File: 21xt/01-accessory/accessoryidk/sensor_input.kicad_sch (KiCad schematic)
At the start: 29 parts, among them IC4 AD7175-8BCPZ-RL7, IC5 INA821IDGKT, IC6 TXB0108PWR, IC8 INA821IDGKT, IC9 INA821IDGKT, J2 Conn_01x25

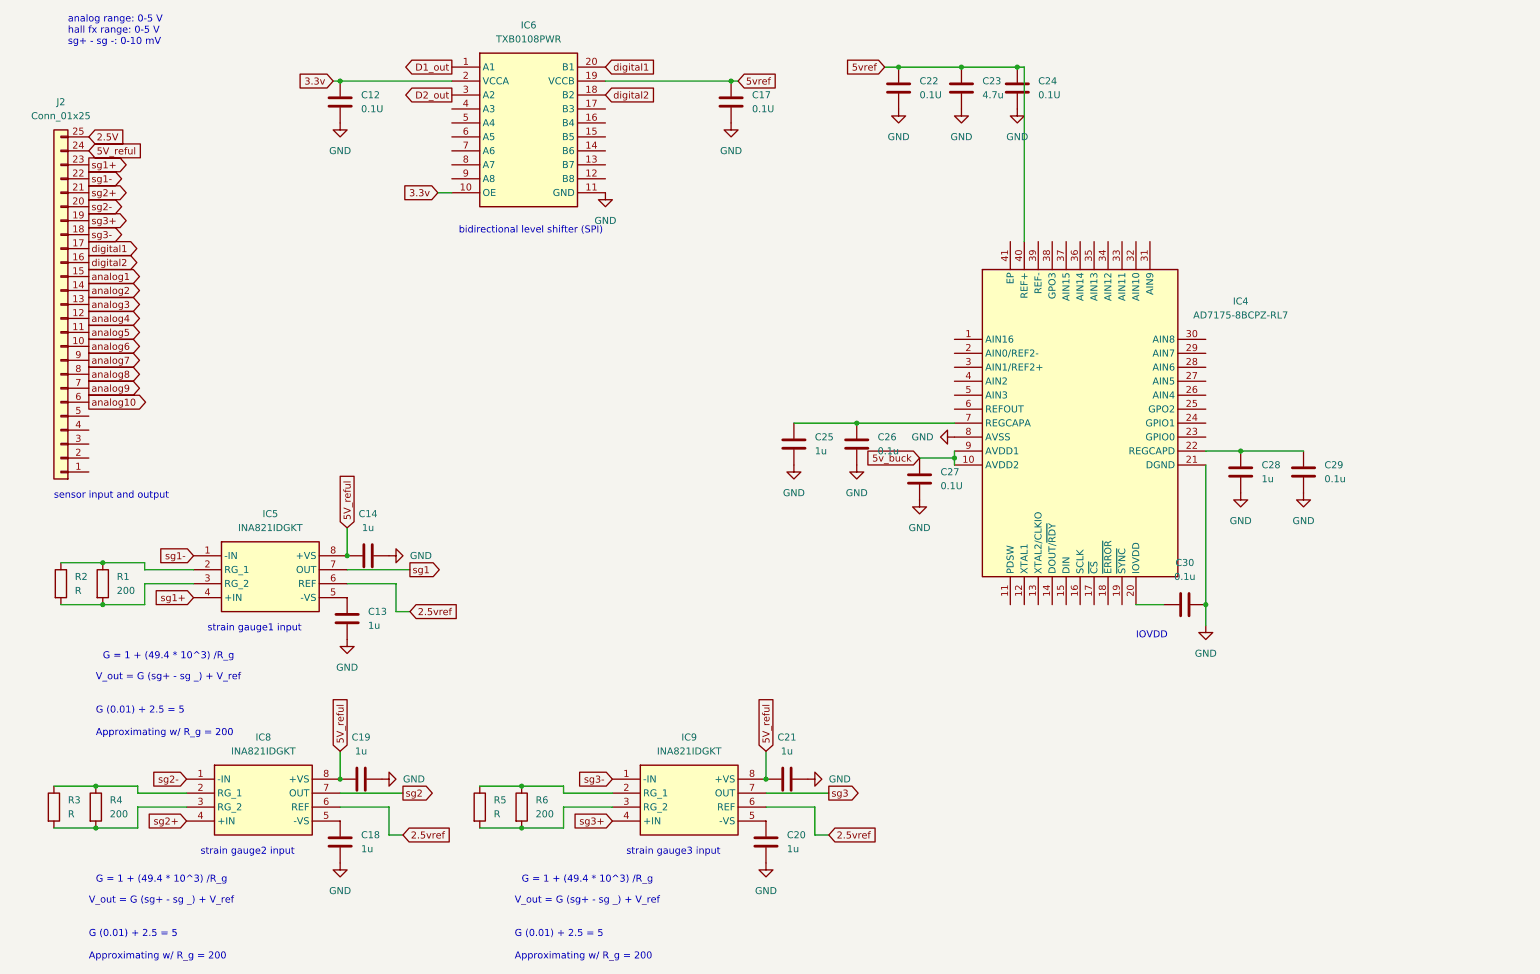
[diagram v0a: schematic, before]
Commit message: Unfinished V1 accessory schematic, remaining teensy connections
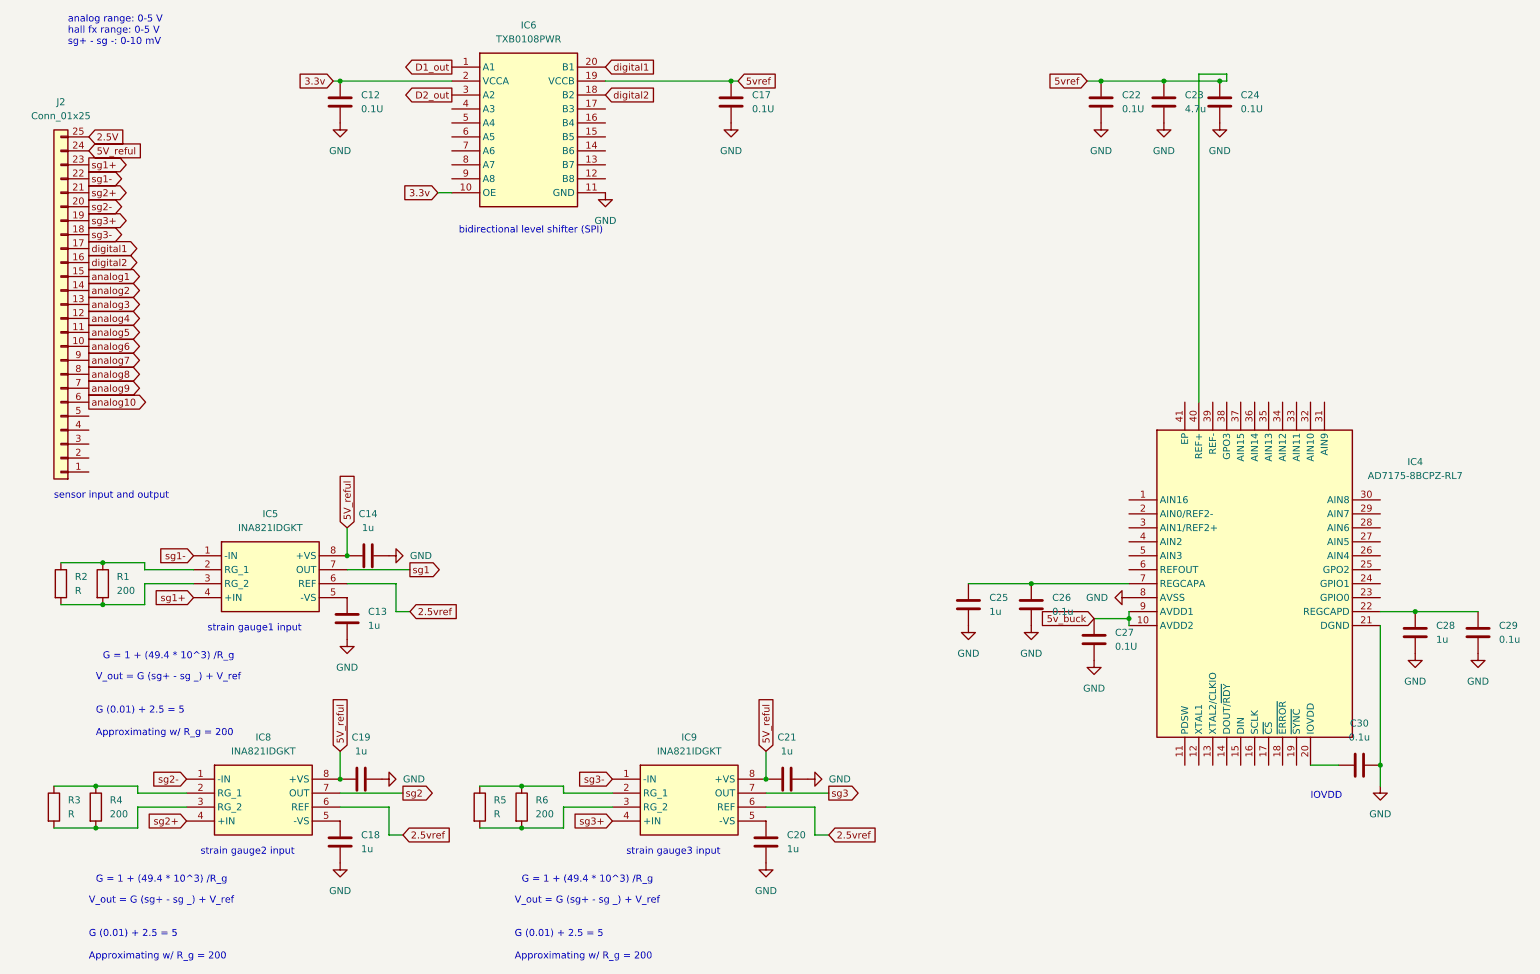
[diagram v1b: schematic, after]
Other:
- moved on the sheet: C22, C23, C24, C25, C26, C27, C28, C29, C30, IC4

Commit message: Unfinished V1 accessory schematic, adding teensy ADC connections part 1
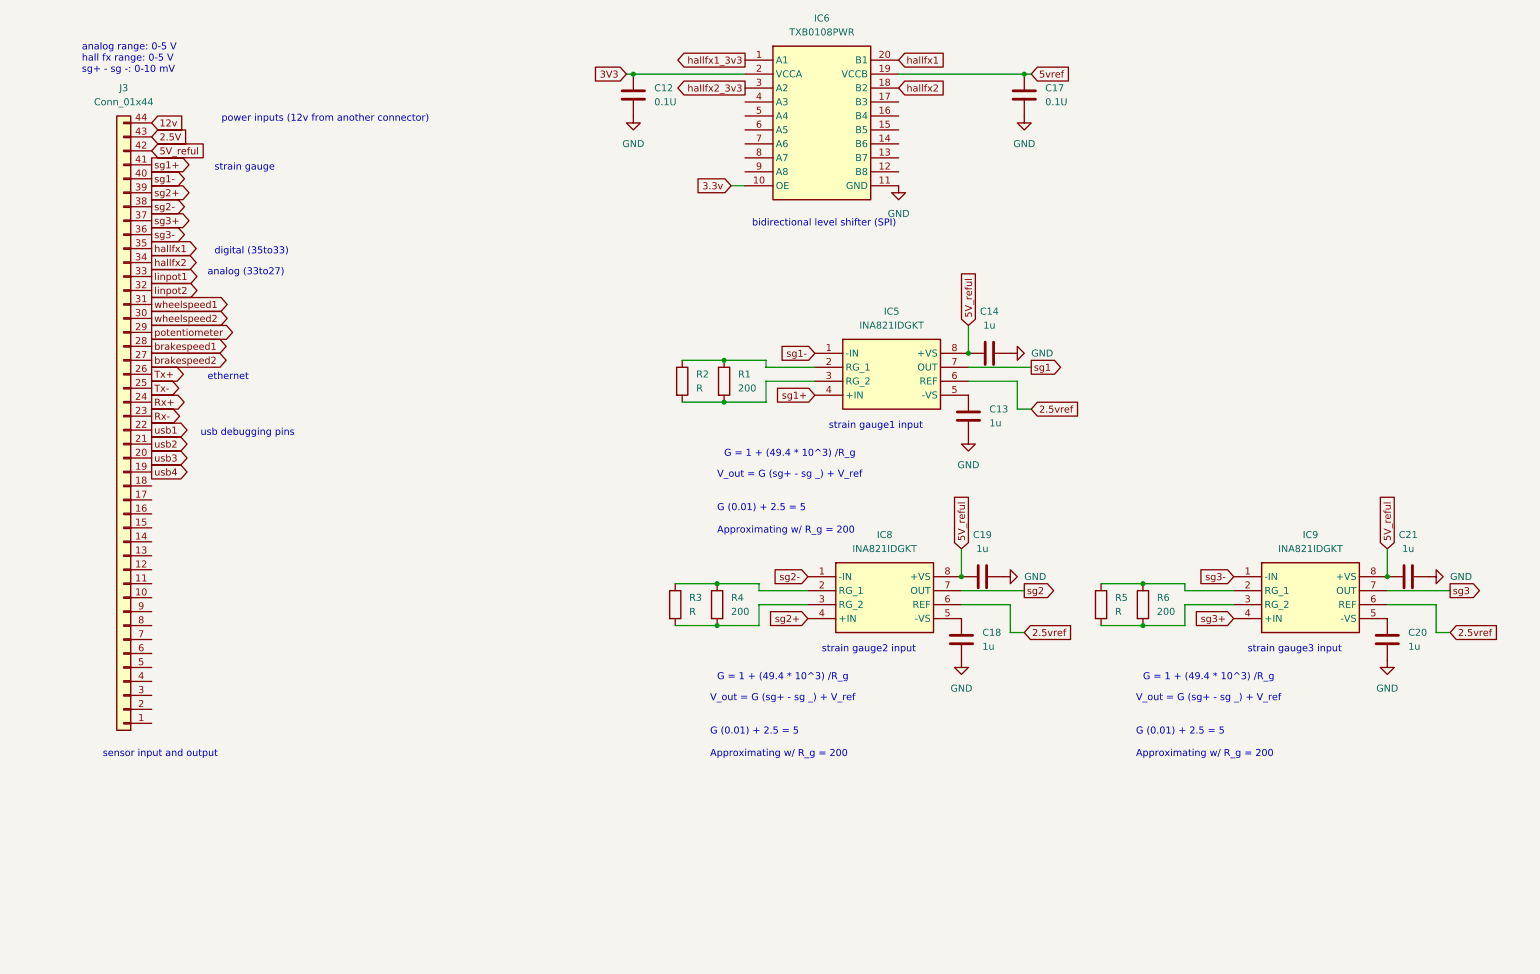
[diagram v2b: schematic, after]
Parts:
- removed C22, C24, C27: 0.1U, symbol Device:C
- removed C23: 4.7u, symbol Device:C
- removed C25, C28: 1u, symbol Device:C
- removed C26, C29, C30: 0.1u, symbol Device:C
- removed IC4: AD7175-8BCPZ-RL7, QFN50P600X600X80-41N-D, symbol 21xt_symbols:AD7175-8BCPZ-RL7
- removed J2: Conn_01x25, symbol Connector_Generic:Conn_01x25
- added J3: Conn_01x44, symbol Connector_Generic:Conn_01x44
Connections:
- net 2.5V: now also J3.43 (Pin_43)
- net 3.3v: no longer C12.1, IC6.2 (VCCA)
- net 5V_reful: now also J3.42 (Pin_42)
- net sg1+: now also J3.41 (Pin_41)
- net sg1-: now also J3.40 (Pin_40)
- net sg2+: now also J3.39 (Pin_39)
- net sg2-: now also J3.38 (Pin_38)
- net sg3+: now also J3.37 (Pin_37)
- net sg3-: now also J3.36 (Pin_36)
- net D1_out renamed hallfx1_3v3
- net D2_out renamed hallfx2_3v3
- net digital1 renamed hallfx1
- net hallfx1: now also J3.35 (Pin_35)
- net digital2 renamed hallfx2
- net hallfx2: now also J3.34 (Pin_34)
- new net 12v: J3.44 (Pin_44)
- new net 3V3: C12.1, IC6.2 (VCCA)
- new net Rx+: J3.24 (Pin_24)
- new net Rx-: J3.23 (Pin_23)
- new net Tx+: J3.26 (Pin_26)
- new net Tx-: J3.25 (Pin_25)
- new net brakespeed1: J3.28 (Pin_28)
- new net brakespeed2: J3.27 (Pin_27)
- new net linpot1: J3.33 (Pin_33)
- new net linpot2: J3.32 (Pin_32)
- new net potentiometer: J3.29 (Pin_29)
- new net usb1: J3.22 (Pin_22)
- new net usb2: J3.21 (Pin_21)
- new net usb3: J3.20 (Pin_20)
- new net usb4: J3.19 (Pin_19)
- new net wheelspeed1: J3.31 (Pin_31)
- new net wheelspeed2: J3.30 (Pin_30)
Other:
- note added: "analog (33to27)"
- note added: "digital (35to33)"
- note added: "ethernet"
- note added: "power inputs (12v from another connector)"
- note added: "strain gauge"
- note added: "usb debugging pins"
- note removed: "IOVDD"
- moved on the sheet: C12, C13, C14, C17, C18, C19, C20, C21, IC5, IC6, IC8, IC9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

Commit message: Finished V1 schematic, adding footprints
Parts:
- added J2: Conn_01x44, symbol Connector_Generic:Conn_01x44
- C12, C17: value 0.1U -> 0.1u; footprint (none) -> Capacitor_SMD:C_0603_1608Metric
- C13, C14, C18, C19, C20, C21: footprint (none) -> Capacitor_SMD:C_0603_1608Metric
- IC5, IC8, IC9: footprint SOP65P490X110-8N -> (none)
- IC6: footprint SOP65P640X120-20N -> (none)
- R1, R2, R3, R4, R5, R6: footprint (none) -> Resistor_SMD:R_0603_1608Metric
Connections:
- net usb1 is gone; now on net sg1-: J3.22 (Pin_22)
- net usb2 is gone; now on net sg2+: J3.21 (Pin_21)
- net usb3 is gone; now on net sg2-: J3.20 (Pin_20)
- net usb4 is gone; now on net sg3+: J3.19 (Pin_19)
- net 12v: now also J2.44 (Pin_44)
- net 2.5V: now also J2.43 (Pin_43)
- net 5V_reful: now also J2.42 (Pin_42)
- net GND: no longer C13.2, C14.2, C18.2, C19.2, C20.2, C21.2
- net Rx+: now also J3.6 (Pin_6), J2.6 (Pin_6); no longer J3.24 (Pin_24)
- net Rx-: now also J3.5 (Pin_5), J2.5 (Pin_5); no longer J3.23 (Pin_23)
- net Tx+: now also J3.8 (Pin_8), J2.8 (Pin_8); no longer J3.26 (Pin_26)
- net Tx-: now also J3.7 (Pin_7), J2.7 (Pin_7); no longer J3.25 (Pin_25)
- net brakespeed1: now also J3.10 (Pin_10), J2.10 (Pin_10); no longer J3.28 (Pin_28)
- net brakespeed2: now also J3.9 (Pin_9), J2.9 (Pin_9); no longer J3.27 (Pin_27)
- net hallfx1: now also J3.17 (Pin_17), J2.17 (Pin_17); no longer J3.35 (Pin_35)
- net hallfx2: now also J3.16 (Pin_16), J2.16 (Pin_16); no longer J3.34 (Pin_34)
- net linpot1: now also J3.15 (Pin_15), J2.15 (Pin_15); no longer J3.33 (Pin_33)
- net linpot2: now also J3.14 (Pin_14), J2.14 (Pin_14); no longer J3.32 (Pin_32)
- net potentiometer: now also J3.11 (Pin_11), J2.11 (Pin_11); no longer J3.29 (Pin_29)
- net sg1+: now also J3.23 (Pin_23), J2.23 (Pin_23); no longer J3.41 (Pin_41)
- net sg1-: now also J2.22 (Pin_22); no longer J3.40 (Pin_40)
- net sg2+: now also J2.21 (Pin_21); no longer J3.39 (Pin_39)
- net sg2-: now also J2.20 (Pin_20); no longer J3.38 (Pin_38)
- net sg3+: now also J2.19 (Pin_19); no longer J3.37 (Pin_37)
- net sg3-: now also J3.18 (Pin_18), J2.18 (Pin_18); no longer J3.36 (Pin_36)
- net wheelspeed1: now also J3.13 (Pin_13), J2.13 (Pin_13); no longer J3.31 (Pin_31)
- net wheelspeed2: now also J3.12 (Pin_12), J2.12 (Pin_12); no longer J3.30 (Pin_30)
- net GNDA: now reaches J3.1 (Pin_1)
- net GNDA: now also C13.2, C14.2, C18.2, C19.2, C20.2, C21.2, J2.1 (Pin_1)
- net usb_d+: now reaches J3.2 (Pin_2)
- net usb_d+: now also J2.2 (Pin_2)
- net usb_d-: now reaches J3.3 (Pin_3)
- net usb_d-: now also J2.3 (Pin_3)
- net 5v_buck: now reaches J3.4 (Pin_4)
- net 5v_buck: now also J2.4 (Pin_4)
- new net GNDD: J2.24 (Pin_24), J2.25 (Pin_25), J2.26 (Pin_26), J2.27 (Pin_27), J2.28 (Pin_28), J2.29 (Pin_29), J2.30 (Pin_30), J2.31 (Pin_31), J2.32 (Pin_32), J2.33 (Pin_33), J2.34 (Pin_34), J2.35 (Pin_35), J2.36 (Pin_36), J2.37 (Pin_37), J2.38 (Pin_38), J2.39 (Pin_39), J2.40 (Pin_40), J2.41 (Pin_41), J3.24 (Pin_24), J3.25 (Pin_25), J3.26 (Pin_26), J3.27 (Pin_27), J3.28 (Pin_28), J3.29 (Pin_29), J3.30 (Pin_30), J3.31 (Pin_31), J3.32 (Pin_32), J3.33 (Pin_33), J3.34 (Pin_34), J3.35 (Pin_35), J3.36 (Pin_36), J3.37 (Pin_37), J3.38 (Pin_38), J3.39 (Pin_39), J3.40 (Pin_40), J3.41 (Pin_41)
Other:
- note added: "sensor input and output (db44)"
- note added: "sensor input and output (dupont testing)"
- note removed: "sensor input and output"
- moved on the sheet: J3

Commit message: Accessory V1 unfinished layout
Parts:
- removed J2, J3: Conn_01x44, symbol Connector_Generic:Conn_01x44
- added J2: DB-44 Connector, 21xt_footprints:23117702, symbol 21xt_symbols:2311770-2
- added J3, J4, J5, J6: Conn_01x11, Connector_JST:JST_EH_B11B-EH-A_1x11_P2.50mm_Vertical, symbol Connector_Generic:Conn_01x11
- IC5, IC8, IC9: footprint (none) -> 21xt_footprints:SOP65P490X110-8N
- IC6: footprint (none) -> 21xt_footprints:SOP65P640X120-20N
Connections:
- net 12v: now also J2.1, J2.16, J2.31, J3.11 (Pin_11)
- net 5v_buck: now also J2.30
- net GNDA: now also J2.44
- net GNDD: now also C12.2, IC6.11 (GND)
- net Rx+: now also J2.29
- net Rx-: now also J2.43
- net Tx+: now also J2.13
- net Tx-: now also J2.28
- net brakespeed1: now also J2.10
- net brakespeed2: now also J2.9
- net hallfx1: now also J2.12
- net hallfx2: now also J2.11
- net linpot1: now also J2.6
- net linpot2: now also J2.22
- net potentiometer: now also J2.8
- net sg1+: now also J2.19
- net sg1-: now also J2.34
- net sg2+: now also J2.4, J3.8 (Pin_8)
- net sg2-: now also J2.20, J3.7 (Pin_7)
- net sg3+: now also J2.5
- net sg3-: now also J2.21
- net usb_d+: now also J2.14
- net usb_d-: now also J2.15
- net wheelspeed1: now also J2.7
- net wheelspeed2: now also J2.37
- net 2.5vref renamed 2.5v_ref
- net 5V_reful renamed 5v_reful
- net 5v_reful: now also J2.3, J3.9 (Pin_9)
- net 5vref renamed 5v_ref
- removed net GND: C12.2, C17.2, IC6.11 (GND)
- new net 2.5v: J2.2, J3.10 (Pin_10)
- new net Earth: C17.2, J2.17, J2.18, J2.23, J2.24, J2.25, J2.26, J2.27, J2.32, J2.33, J2.35, J2.36, J2.38, J2.39, J2.40, J2.41, J2.42, J2.MH1, J2.MH2
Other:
- note removed: "analog (33to27)"
- note removed: "digital (35to33)"
- note removed: "ethernet"
- note removed: "strain gauge"
- note removed: "usb debugging pins"

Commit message: Finished Accessory V1 schematic, need DRC checks
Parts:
- removed J2: DB-44 Connector, 21xt_footprints:23117702, symbol 21xt_symbols:2311770-2
- removed J6: Conn_01x11, Connector_JST:JST_EH_B11B-EH-A_1x11_P2.50mm_Vertical, symbol Connector_Generic:Conn_01x11
- added J2: 5747847-6, 21xt_footprints:57478476, symbol 21xt_symbols:5747847-6
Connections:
- net 3.3v is gone; now on net 3V3: IC6.10 (OE)
- net GNDA is gone; now on net GND: C13.2, C14.2, C18.2, C19.2, C20.2, C21.2
- net 12v: now also J3.10 (Pin_10), J3.9 (Pin_9), J2.1, J2.20, J2.21
- net 2.5v: now also J3.7 (Pin_7), J2.22; no longer J3.10 (Pin_10)
- net 5v_buck: now also J5.3 (Pin_3), J2.19
- net 5v_reful: now also J3.8 (Pin_8), J2.2; no longer J3.9 (Pin_9)
- net Earth: now also C12.2, J4.8 (Pin_8), J2.10, J2.11, J2.12, J2.13, J2.29, J2.30, J2.31, J2.32, J2.MH1, J2.MH2
- net GNDD: now also J4.9 (Pin_9), J2.14; no longer C12.2
- net Rx+: now also J5.7 (Pin_7), J2.16
- net Rx-: now also J5.8 (Pin_8), J2.34
- net Tx+: now also J5.5 (Pin_5), J2.17
- net Tx-: now also J5.6 (Pin_6), J2.35
- net brakespeed1: now also J4.6 (Pin_6), J2.28
- net brakespeed2: now also J4.7 (Pin_7), J2.9
- net hallfx1: now also J4.11 (Pin_11), J2.15
- net hallfx2: now also J4.10 (Pin_10), J2.33
- net linpot1: now also J4.1 (Pin_1), J2.6
- net linpot2: now also J4.2 (Pin_2), J2.26
- net potentiometer: now also J4.5 (Pin_5), J2.8
- net sg1+: now also J3.6 (Pin_6), J2.3
- net sg1-: now also J3.5 (Pin_5), J2.23
- net sg2+: now also J3.4 (Pin_4), J2.4; no longer J3.8 (Pin_8)
- net sg2-: now also J3.3 (Pin_3), J2.24; no longer J3.7 (Pin_7)
- net sg3+: now also J3.2 (Pin_2), J2.5
- net sg3-: now also J3.1 (Pin_1), J2.25
- net usb_d+: now also J5.1 (Pin_1), J2.36
- net usb_d-: now also J5.2 (Pin_2), J2.18
- net wheelspeed1: now also J4.3 (Pin_3), J2.7
- net wheelspeed2: now also J4.4 (Pin_4), J2.27
- net GND: now reaches J5.4 (Pin_4)
- net GND: now also J2.37
- no-connect marks 0 -> 15
